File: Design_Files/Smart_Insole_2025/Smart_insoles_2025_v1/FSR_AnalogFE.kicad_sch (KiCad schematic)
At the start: 33 parts, among them J1 Conn_01x20, U8 MCP6004-I_ST, U9 MCP6004-I_ST

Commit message: SCH: Added missing footprints. PCB: Grouped related components for new layout
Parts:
- C10, C11, C12, C13, C6, C7, C8, C9: footprint Capacitor_SMD:C_0603_1608Metric_Pad1.08x0.95mm_HandSolder -> Capacitor_SMD:C_0805_2012Metric
- C17, C18, C4, C5: footprint Capacitor_SMD:C_0603_1608Metric_Pad1.08x0.95mm_HandSolder -> Capacitor_SMD:C_0805_2012Metric_Pad1.18x1.45mm_HandSolder
- R3, R4: footprint Resistor_SMD:R_0603_1608Metric_Pad0.98x0.95mm_HandSolder -> Resistor_SMD:R_0805_2012Metric
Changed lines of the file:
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@@
 			)
 		)
-		(property "Footprint" "Capacitor_SMD:C_0603_1608Metric_Pad1.08x0.95mm_HandSolder"
+		(property "Footprint" "Capacitor_SMD:C_0805_2012Metric_Pad1.18x1.45mm_HandSolder"
 			(at 209.55 104.4448 0)
 			(effects
@@
 			)
 		)
-		(property "Footprint" "Capacitor_SMD:C_0603_1608Metric_Pad1.08x0.95mm_HandSolder"
+		(property "Footprint" "Capacitor_SMD:C_0805_2012Metric"
 			(at 101.6 35.8648 0)
 			(effects
@@
 			)
 		)
-		(property "Footprint" "Capacitor_SMD:C_0603_1608Metric_Pad1.08x0.95mm_HandSolder"
+		(property "Footprint" "Capacitor_SMD:C_0805_2012Metric_Pad1.18x1.45mm_HandSolder"
 			(at 182.5752 36.83 0)
 			(effects
@@
 			)
 		)
-		(property "Footprint" "Capacitor_SMD:C_0603_1608Metric_Pad1.08x0.95mm_HandSolder"
+		(property "Footprint" "Capacitor_SMD:C_0805_2012Metric"
 			(at 60.96 106.9848 0)
 			(effects
@@
 			)
 		)
-		(property "Footprint" "Resistor_SMD:R_0603_1608Metric_Pad0.98x0.95mm_HandSolder"
+		(property "Footprint" "Resistor_SMD:R_0805_2012Metric"
 			(at 39.878 29.21 90)
 			(effects
@@
 			)
 		)
-		(property "Footprint" "Capacitor_SMD:C_0603_1608Metric_Pad1.08x0.95mm_HandSolder"
+		(property "Footprint" "Capacitor_SMD:C_0805_2012Metric"
 			(at 60.96 35.8648 0)
 			(effects
@@
 			)
 		)
-		(property "Footprint" "Capacitor_SMD:C_0603_1608Metric_Pad1.08x0.95mm_HandSolder"
+		(property "Footprint" "Capacitor_SMD:C_0805_2012Metric_Pad1.18x1.45mm_HandSolder"
 			(at 265.1252 36.83 0)
 			(effects
@@
 			)
 		)
-		(property "Footprint" "Capacitor_SMD:C_0603_1608Metric_Pad1.08x0.95mm_HandSolder"
+		(property "Footprint" "Capacitor_SMD:C_0805_2012Metric"
 			(at 104.14 103.1748 0)
 			(effects
@@
 			)
 		)
-		(property "Footprint" "Capacitor_SMD:C_0603_1608Metric_Pad1.08x0.95mm_HandSolder"
+		(property "Footprint" "Capacitor_SMD:C_0805_2012Metric"
 			(at 106.68 57.4548 0)
 			(effects
@@
 			)
 		)
-		(property "Footprint" "Capacitor_SMD:C_0603_1608Metric_Pad1.08x0.95mm_HandSolder"
+		(property "Footprint" "Capacitor_SMD:C_0805_2012Metric"
 			(at 60.96 58.7248 0)
 			(effects
@@
 			)
 		)
-		(property "Footprint" "Capacitor_SMD:C_0603_1608Metric_Pad1.08x0.95mm_HandSolder"
+		(property "Footprint" "Capacitor_SMD:C_0805_2012Metric"
 			(at 107.95 81.5848 0)
 			(effects
@@
 			)
 		)
-		(property "Footprint" "Capacitor_SMD:C_0603_1608Metric_Pad1.08x0.95mm_HandSolder"
+		(property "Footprint" "Capacitor_SMD:C_0805_2012Metric_Pad1.18x1.45mm_HandSolder"
 			(at 186.3852 97.79 0)
 			(effects
@@
 			)
 		)
-		(property "Footprint" "Capacitor_SMD:C_0603_1608Metric_Pad1.08x0.95mm_HandSolder"
+		(property "Footprint" "Capacitor_SMD:C_0805_2012Metric"
 			(at 60.96 81.5848 0)
 			(effects
@@
 			)
 		)
-		(property "Footprint" "Resistor_SMD:R_0603_1608Metric_Pad0.98x0.95mm_HandSolder"
+		(property "Footprint" "Resistor_SMD:R_0805_2012Metric"
 			(at 39.878 49.53 90)
 			(effects

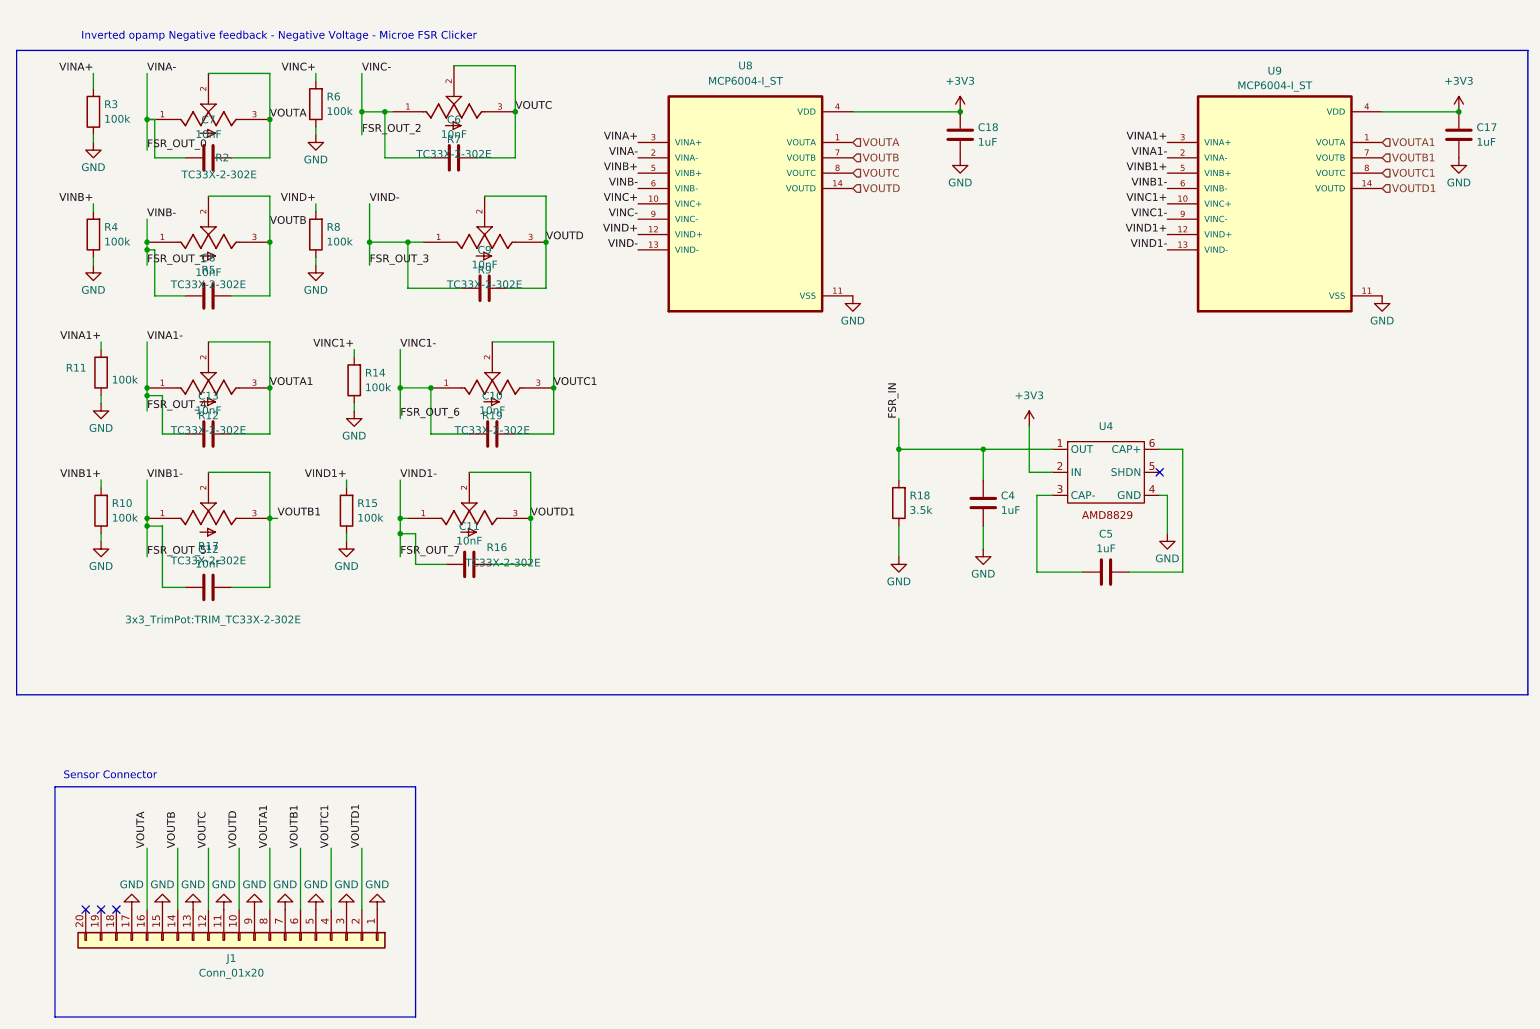
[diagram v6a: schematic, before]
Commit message: SCH: Fixed Warnings. Added thermistor solder pads library.
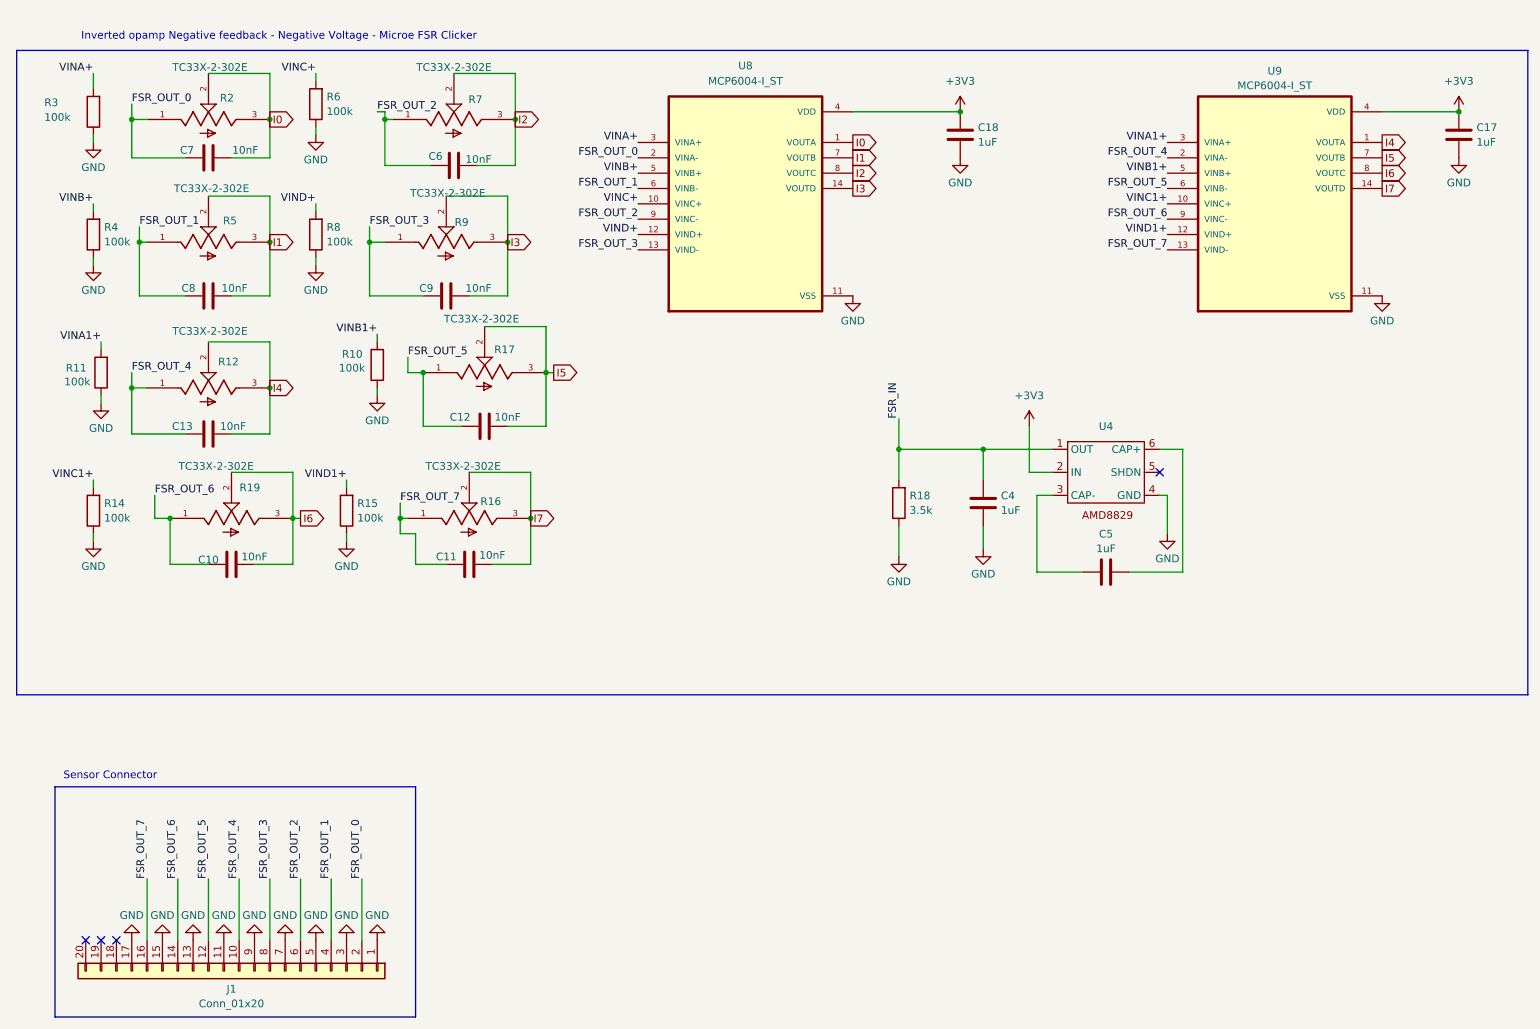
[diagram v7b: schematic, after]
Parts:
- R10, R11, R14, R15, R18, R6: footprint Resistor_SMD:R_0603_1608Metric_Pad0.98x0.95mm_HandSolder -> Resistor_SMD:R_0805_2012Metric
- R8: footprint Resistor_SMD:R_0603_1608Metric_Pad0.98x0.95mm_HandSolder -> Resistor_SMD:R_0805_2012Metric_Pad1.20x1.40mm_HandSolder
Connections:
- net FSR_OUT_0: now also J1.2 (Pin_2)
- net FSR_OUT_1: now also J1.4 (Pin_4)
- net FSR_OUT_2: now also J1.6 (Pin_6)
- net FSR_OUT_3: now also J1.8 (Pin_8)
- net FSR_OUT_4: now also J1.10 (Pin_10)
- net FSR_OUT_5: now also J1.12 (Pin_12)
- net FSR_OUT_6: now also J1.14 (Pin_14)
- net FSR_OUT_7: now also J1.16 (Pin_16)
- net VOUTA renamed I0
- net I0: no longer J1.16 (Pin_16)
- net VOUTA1 renamed I4
- net I4: no longer J1.8 (Pin_8)
- net VOUTB renamed I1
- net I1: no longer J1.14 (Pin_14)
- net VOUTB1 renamed I5
- net I5: no longer J1.6 (Pin_6)
- net VOUTC renamed I2
- net I2: no longer J1.12 (Pin_12)
- net VOUTC1 renamed I6
- net I6: no longer J1.4 (Pin_4)
- net VOUTD renamed I3
- net I3: no longer J1.10 (Pin_10)
- net VOUTD1 renamed I7
- net I7: no longer J1.2 (Pin_2)
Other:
- moved on the sheet: C10, C12, C6, C9, J1, R10, R14, R17, R19, R7, R9

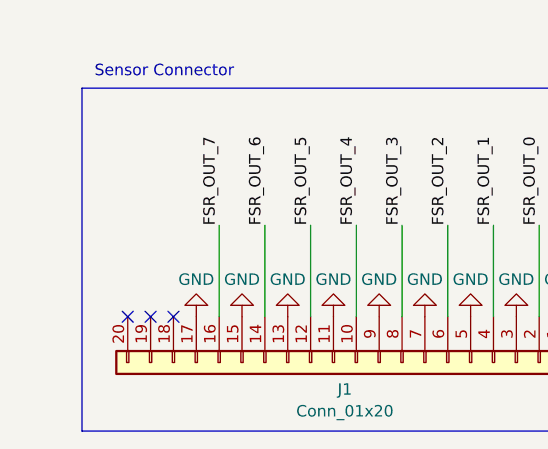
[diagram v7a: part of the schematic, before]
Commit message: SCH: Added FSR_In missing connections.
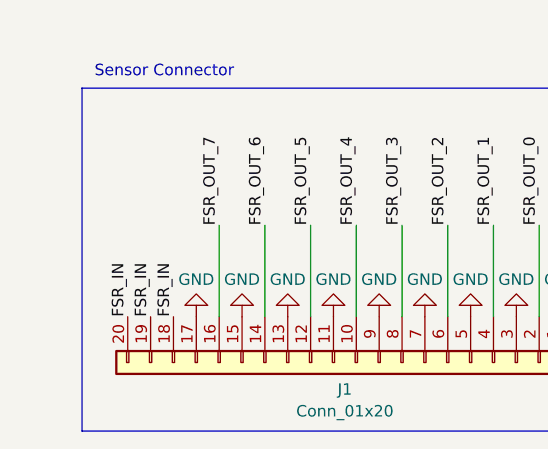
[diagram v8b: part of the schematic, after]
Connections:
- net FSR_IN: now also J1.18 (Pin_18), J1.19 (Pin_19), J1.20 (Pin_20)
- no-connect marks 4 -> 1
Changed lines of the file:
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@@
-	)
-	(no_connect
-		(at 41.91 166.37)
 	)
 	(no_connect
 		(at 214.63 88.9)
 	)
-	(no_connect
-		(at 39.37 166.37)
-	)
-	(no_connect
-		(at 36.83 166.37)
-	)
 	(wire
 		(pts
@@
 		)
 	)
+	(label "FSR_IN"
+		(at 39.37 166.37 90)
+		(effects
+			(font
+				(size 1.27 1.27)
+			)
+			(justify left bottom)
+		)
+	)
+	(label "FSR_IN"
+		(at 41.91 166.37 90)
+		(effects
+			(font
+				(size 1.27 1.27)
+			)
+			(justify left bottom)
+		)
+	)
 	(label "FSR_OUT_2"
 		(at 128.27 46.99 180)
@@
 		)
 	)
+	(label "FSR_IN"
+		(at 36.83 166.37 90)
+		(effects
+			(font
+				(size 1.27 1.27)
+			)
+			(justify left bottom)
+		)
+	)
